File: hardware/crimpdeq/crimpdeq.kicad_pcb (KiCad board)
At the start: 2 copper layers, 54 parts, among them J2 USB4105-GF-A, Q1 S8550, Q2 DMG3415U, SW1 SW_Push, SW2 SW_Push, U1 ESP32-C3-MINI-1, U2 MCP73831T-2ACI/OT, U3 HX711, U4 Rust_Board, U6 SY8088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

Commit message: pcb: Initial placing of hx711
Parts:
- moved C10 114.2 mm to (142.5, 83.5)
- moved C9 112.8 mm to (139.2, 83.5)
- moved C12 108.5 mm to (143.8, 74.2), turned to 90 degrees
- moved C11 108.2 mm to (143.8, 71.0), turned to -90 degrees
- moved C13 106.0 mm to (144.6, 68.4), turned to 180 degrees
- moved R7 104.0 mm to (145.2, 74.8), turned to 90 degrees
- moved R8 103.8 mm to (145.8, 69.8), turned to 180 degrees
- moved R6 102.3 mm to (142.2, 77.0)
- moved R5 100.4 mm to (139.5, 77.0)
- moved J2 99.3 mm to (140.7, 104.4), turned to 180 degrees
- moved Q1 92.8 mm to (139.5, 80.5)
- moved U3 91.7 mm to (137.6, 72.4), turned to 90 degrees
- moved R10 8.25 mm to (147.0, 74.6), turned to 180 degrees
- moved C14 3.50 mm to (147.0, 75.8), turned to 180 degrees
- moved SW2 1.74 mm to (146.0, 80.0)
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
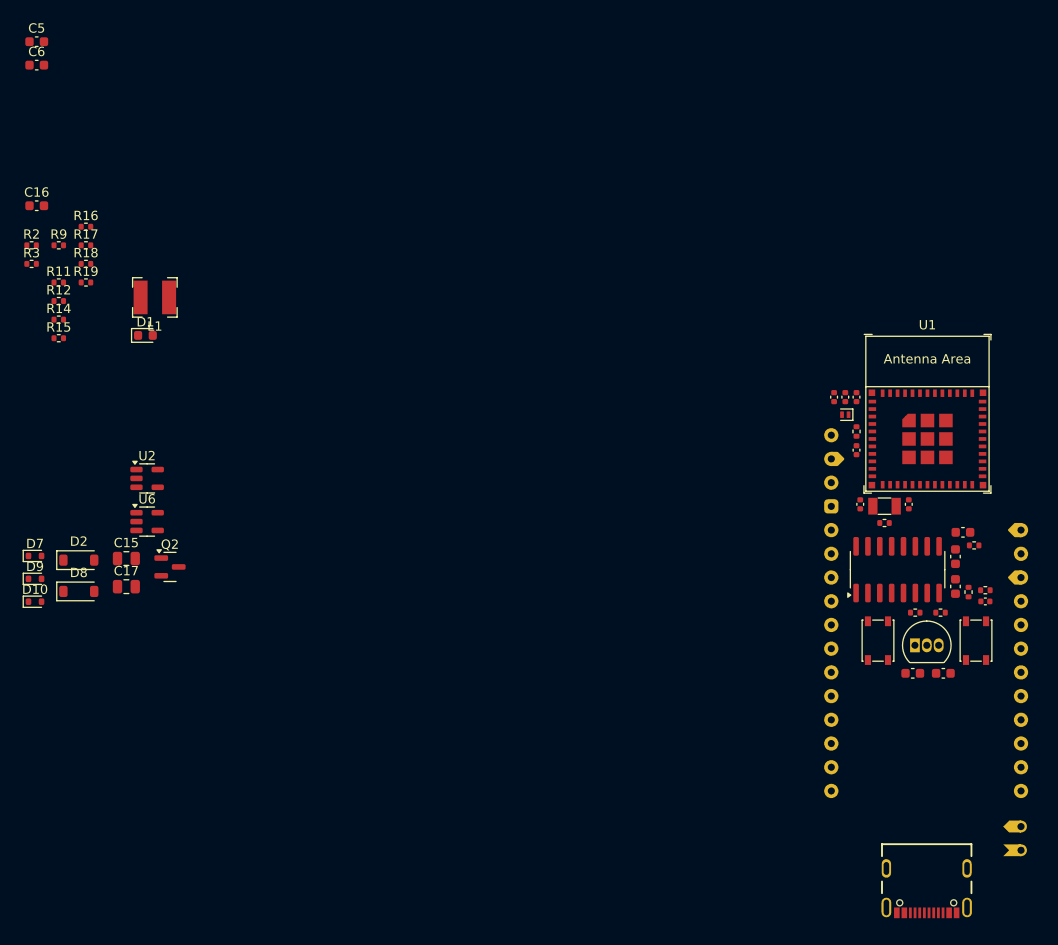
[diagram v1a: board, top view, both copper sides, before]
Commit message: pcb: Initial wiring of pcb
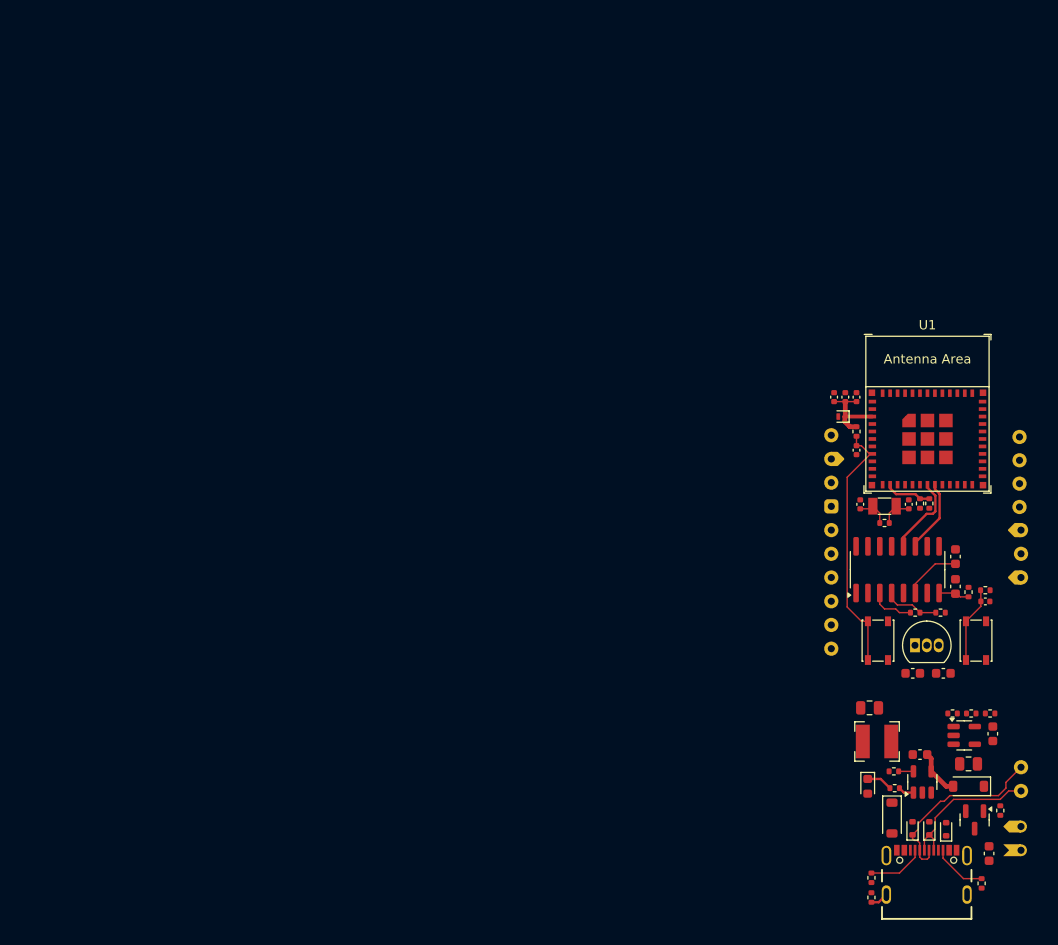
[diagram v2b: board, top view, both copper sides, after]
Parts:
- removed C13: 0.1uF, Capacitor_SMD:C_0603_1608Metric
- removed R8: 1kR 1%, Resistor_SMD:R_0402_1005Metric
- moved C6 132.4 mm to (147.4, 102.8), turned to -90 degrees
- moved C5 121.6 mm to (140.0, 92.2)
- moved R9 117.6 mm to (148.6, 98.2), turned to -90 degrees
- moved C16 117.0 mm to (147.8, 90.0), turned to -90 degrees
- moved R18 116.6 mm to (146.6, 106.0), turned to -90 degrees
- moved R17 109.3 mm to (134.8, 107.5), turned to 90 degrees
- moved R16 108.2 mm to (145.5, 87.8), turned to 180 degrees
- moved R2 108.2 mm to (137.2, 94.0)
- moved R3 108.2 mm to (137.3, 95.8), turned to 180 degrees
- moved R15 107.5 mm to (147.5, 87.8), turned to 180 degrees
- moved R19 105.6 mm to (134.8, 105.4), turned to -90 degrees
- moved R14 104.6 mm to (143.5, 87.8), turned to 180 degrees
- moved D9 101.2 mm to (142.8, 100.2), turned to 90 degrees
- moved D10 98.8 mm to (141.0, 100.1), turned to 90 degrees
- moved D7 98.4 mm to (139.2, 100.1), turned to 90 degrees
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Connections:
- C1 pad 2: GND -> E-
- C10 pad 1: Net-(Q1-C) -> E+
- C10 pad 2: GND -> E-
- C11 pad 1: GND -> E-
- C14 pad 1: GND -> E-
- C15 pad 2: GND -> E-
- C17 pad 2: GND -> E-
- C2 pad 2: GND -> E-
- C3 pad 2: GND -> E-
- C4 pad 2: GND -> E-
- C5 pad 1: GND -> E-
- C6 pad 2: GND -> E-
- C7 pad 2: GND -> E-
- C8 pad 2: GND -> E-
- C9 pad 2: GND -> E-
- D10 pad 2: GND -> E-
- D3 pad 2: GND -> E-
- D7 pad 2: GND -> E-
- D9 pad 2: GND -> E-
- J2 pad A1_B12: GND -> E-
- J2 pad B1_A12: GND -> E-
- Q1 pad 3: Net-(Q1-C) -> E+
- R11 pad 2: GND -> E-
- R16 pad 2: GND -> E-
- R17 pad 2: GND -> E-
- R18 pad 2: GND -> E-
- R19 pad 2: GND -> E-
- R2 pad 1: GND -> E-
- R5 pad 1: Net-(Q1-C) -> E+
- R6 pad 2: GND -> E-
- R9 pad 2: GND -> E-
- SW1 pad 2: GND -> E-
- SW2 pad 2: GND -> E-
- U1 pad 1: GND -> E-
- U1 pad 11: GND -> E-
- U1 pad 12: IO0 -> unconnected-(U1-GPIO0/ADC1_CH0/XTAL_32K_P-Pad12)
- U1 pad 14: GND -> E-
- U1 pad 16: IO10 -> unconnected-(U1-GPIO10-Pad16)
- U1 pad 2: GND -> E-
- U1 pad 20: IO6 -> unconnected-(U1-GPIO6-Pad20)
- U1 pad 21: IO7 -> unconnected-(U1-GPIO7-Pad21)
- U1 pad 22: IO8 -> unconnected-(U1-GPIO8-Pad22)
- U1 pad 36: GND -> E-
- U1 pad 5: IO2 -> unconnected-(U1-GPIO2/ADC1_CH2-Pad5)
- U1 pad 6: IO3 -> unconnected-(U1-GPIO3/ADC1_CH3-Pad6)
- U2 pad 2: GND -> E-
- U3 pad 10: Net-(U3-INB+) -> E-
- U3 pad 14: GND -> E-
- U3 pad 15: GND -> E-
- U3 pad 3: Net-(Q1-C) -> E+
- U3 pad 5: GND -> E-
- U3 pad 9: B- -> E-
- U4 pad 10: IO5_SCK -> IO9_BOOT
- U4 pad 11: IO6 -> USB_D+
- U4 pad 12: IO7 -> USB_D-
- U4 pad 13: IO8 -> VBUS
- U4 pad 14: IO21_TX -> ENABLE
- U4 pad 15: IO20_RX -> +BATT
- U4 pad 16: IO9_BOOT -> A+
- U4 pad 17: IO10 -> A-
- U4 pad 18: IO8 -> E-
- U4 pad 19: USB_D+ -> E+
- U4 pad 20: USB_D- -> E-
- U4 pad 21: unconnected-(U4-SPIQ/GPIO17-Pad21) -> +BATT
- U4 pad 4: GND -> E-
- U4 pad 5: IO0 -> IO1_ADC
- U4 pad 6: IO1_ADC -> IO4_DATA
- U4 pad 7: IO2 -> IO5_SCK
- U4 pad 8: IO3 -> IO21_TX
- U4 pad 9: IO4_DATA -> IO20_RX
- U6 pad 2: GND -> E-
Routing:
- net CHIP_PU: track 0.00 -> 27.7 mm
- net USB_D-: track 0.00 -> 20.1 mm
- net USB_D+: track 0.00 -> 16.2 mm
- net +3V3: track 0.00 -> 8.99 mm
- net IO4_DATA: track 0.00 -> 8.75 mm
- net IO9_BOOT: track 0.00 -> 8.15 mm
- net IO5_SCK: track 0.00 -> 7.88 mm
- net Net-(U3-VBG): track 0.00 -> 6.18 mm
- net Net-(J2-CC1): track 0.00 -> 6.14 mm
- net Net-(U3-VFB): track 0.00 -> 5.98 mm
- net Net-(J2-CC2): track 0.00 -> 5.89 mm
- net IO1_ADC: track 0.00 -> 5.04 mm
- net VBUS: track 0.00 -> 4.99 mm
- net E+: track 0.00 -> 4.85 mm
- net IO1: track 0.00 -> 3.57 mm
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
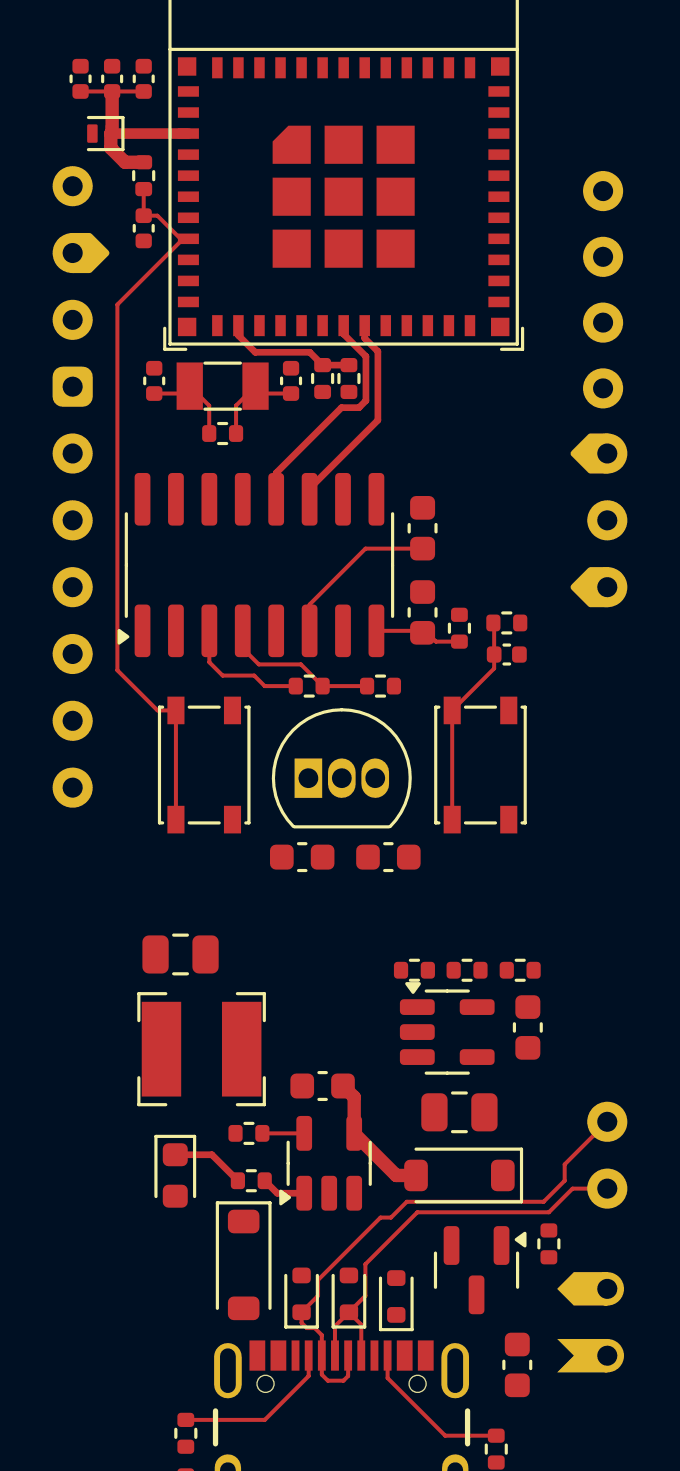
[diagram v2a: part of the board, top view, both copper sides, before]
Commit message: pcb: Remove unused exposed pins and connect hx711/RATE to 3.3v
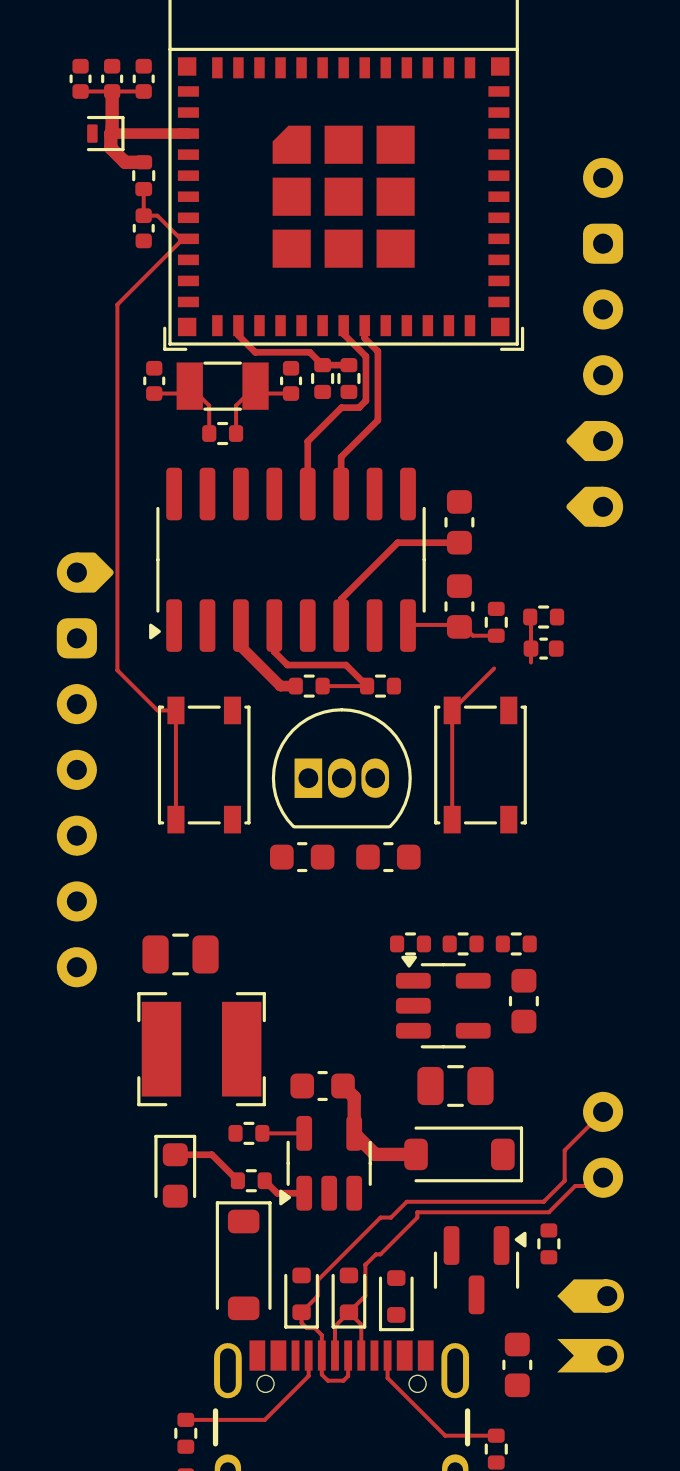
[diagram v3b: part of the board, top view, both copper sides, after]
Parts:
- moved C14 1.42 mm to (148.4, 75.6)
- moved R10 1.42 mm to (148.4, 74.4)
- moved R7 1.42 mm to (146.6, 74.6)
- moved C12 1.42 mm to (145.2, 74.0)
- moved C11 1.42 mm to (145.2, 70.8)
- moved U3 1.22 mm to (138.8, 72.2)
- moved C16 1.01 mm to (147.7, 89.0)
- moved R14 1.01 mm to (143.3, 86.8)
- moved R16 1.01 mm to (145.3, 86.8)
- moved U6 1.01 mm to (144.6, 89.2)
- moved C15 1.01 mm to (145.1, 92.2)
- moved R15 1.01 mm to (147.4, 86.8)
- moved D2 0.80 mm to (145.2, 94.8)
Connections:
- C1 pad 2: E- -> GND
- C10 pad 2: E- -> GND
- C11 pad 1: E- -> GND
- C14 pad 1: E- -> GND
- C15 pad 2: E- -> GND
- C17 pad 2: E- -> GND
- C2 pad 2: E- -> GND
- C3 pad 2: E- -> GND
- C4 pad 2: E- -> GND
- C5 pad 1: E- -> GND
- C6 pad 2: E- -> GND
- C7 pad 2: E- -> GND
- C8 pad 2: E- -> GND
- C9 pad 1: +3.3V -> +3V3
- C9 pad 2: E- -> GND
- D10 pad 2: E- -> GND
- D3 pad 2: E- -> GND
- D7 pad 2: E- -> GND
- D9 pad 2: E- -> GND
- J2 pad A1_B12: E- -> GND
- J2 pad B1_A12: E- -> GND
- Q1 pad 1: +3.3V -> +3V3
- R11 pad 2: E- -> GND
- R16 pad 2: E- -> GND
- R17 pad 2: E- -> GND
- R18 pad 2: E- -> GND
- R19 pad 2: E- -> GND
- R2 pad 1: E- -> GND
- R6 pad 2: E- -> GND
- R9 pad 2: E- -> GND
- SW1 pad 2: E- -> GND
- SW2 pad 2: E- -> GND
- U1 pad 1: E- -> GND
- U1 pad 11: E- -> GND
- U1 pad 14: E- -> GND
- U1 pad 2: E- -> GND
- U1 pad 36: E- -> GND
- U1 pad 49: (no net) -> GND
- U2 pad 2: E- -> GND
- U3 pad 1: +3.3V -> +3V3
- U3 pad 10: E- -> GND
- U3 pad 14: E- -> GND
- U3 pad 15: E- -> +3V3
- U3 pad 16: +3.3V -> +3V3
- U3 pad 5: E- -> GND
- U3 pad 9: E- -> GND
- U4 pad 1: CHIP_PU -> +3V3
- U4 pad 10: IO9_BOOT -> VBUS
- U4 pad 11: USB_D+ -> +BATT
- U4 pad 12: USB_D- -> A+
- U4 pad 13: VBUS -> A-
- U4 pad 14: ENABLE -> GND
- U4 pad 15: +BATT -> E+
- U4 pad 16: A+ -> GND
- U4 pad 17: A- -> +BATT
- U4 pad 2: +3V3 -> GND
- U4 pad 3: unconnected-(U4-N/C-Pad3) -> IO1_ADC
- U4 pad 4: E- -> IO4_DATA
- U4 pad 5: IO1_ADC -> IO5_SCK
- U4 pad 6: IO4_DATA -> IO21_TX
- U4 pad 7: IO5_SCK -> IO20_RX
- U4 pad 8: IO21_TX -> USB_D-
- U4 pad 9: IO20_RX -> USB_D+
- U6 pad 2: E- -> GND
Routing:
- net unconnected-(U3-XO-Pad13): track 0.00 -> 1.00 mm
- net GND: track 0.00 -> 1.00 mm
- net Net-(U3-VFB): track 5.98 -> 6.75 mm
- net IO5_SCK: track 7.88 -> 7.19 mm
- net E+: track 4.85 -> 4.17 mm
- net VBUS: track 4.99 -> 4.48 mm

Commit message: pcb: Update layout
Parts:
- moved R12 1.62 mm to (139.8, 66.4)
- moved R11 0.65 mm to (140.4, 64.8), turned to 0 degrees
- moved R16 0.40 mm to (145.3, 86.4), turned to 90 degrees
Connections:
- U1 pad 49: GND -> (no net)
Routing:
- net +BATT: track 0.00 -> 69.7 mm, vias 0 -> 6
- net +3V3: track 8.99 -> 77.7 mm, vias 0 -> 1
- net USB_D+: track 16.3 -> 55.2 mm, vias 0 -> 5
- net USB_D-: track 20.5 -> 57.7 mm, vias 0 -> 5
- net VBUS: track 4.48 -> 36.9 mm, vias 0 -> 3
- net E+: track 4.17 -> 22.0 mm, vias 0 -> 1
- net GND: track 1.00 -> 18.2 mm, vias 0 -> 7
- net Net-(D8-A): track 0.00 -> 16.4 mm, vias 0 -> 2
- net IO9_BOOT: track 8.15 -> 22.0 mm, vias 0 -> 2
- net +5V: track 0.00 -> 13.5 mm
- net IO4_DATA: track 8.47 -> 20.4 mm, vias 0 -> 1
- net A-: track 0.00 -> 11.1 mm
- net IO5_SCK: track 7.19 -> 16.2 mm
- net Net-(Q1-B): track 0.00 -> 8.49 mm
- net IO1_ADC: track 5.04 -> 12.4 mm, vias 0 -> 1
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- added copper zone on F.Cu, net +3V3
- added copper zone on F.Cu, net +5V
- added copper zone on F.Cu, net +BATT
- added copper zone on F.Cu, net /Buck_Coil
- added copper zone on B.Cu, net GND
- added copper zone on F.Cu, net GND

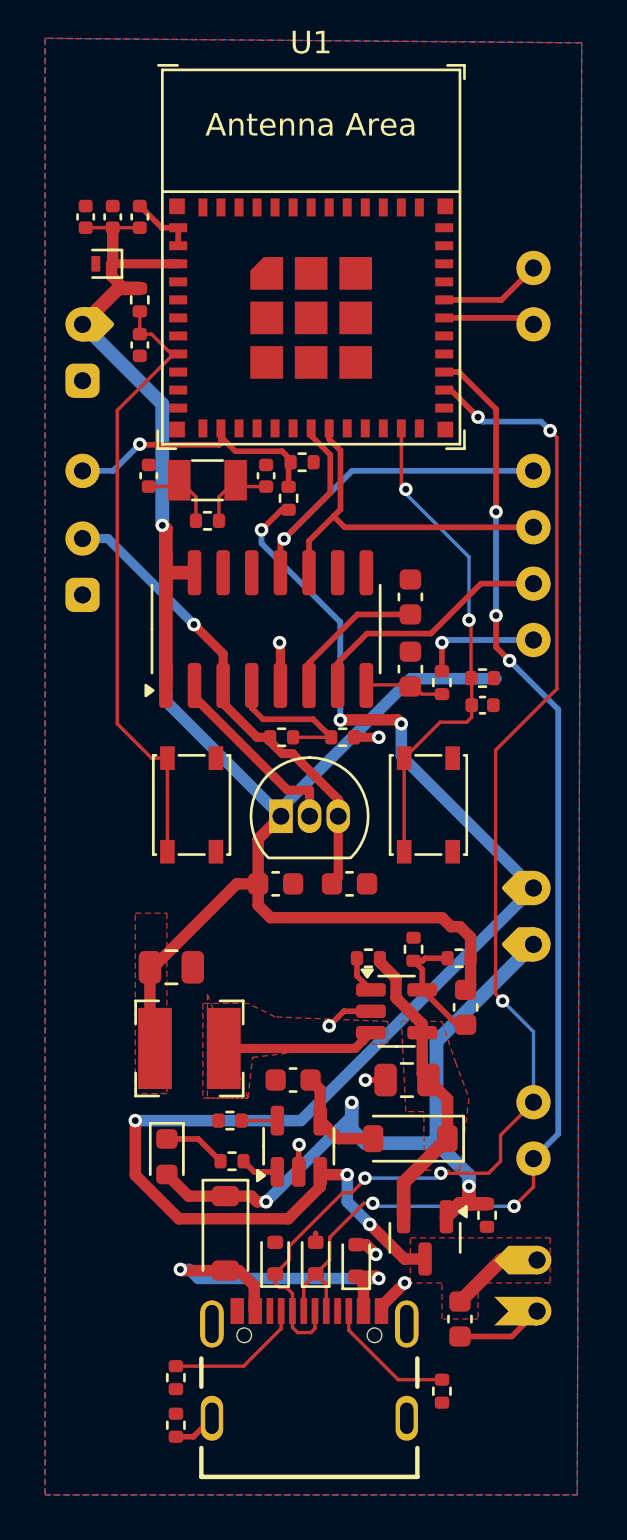
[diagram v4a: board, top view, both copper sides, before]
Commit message: pcb: Fix DRC unconnected items
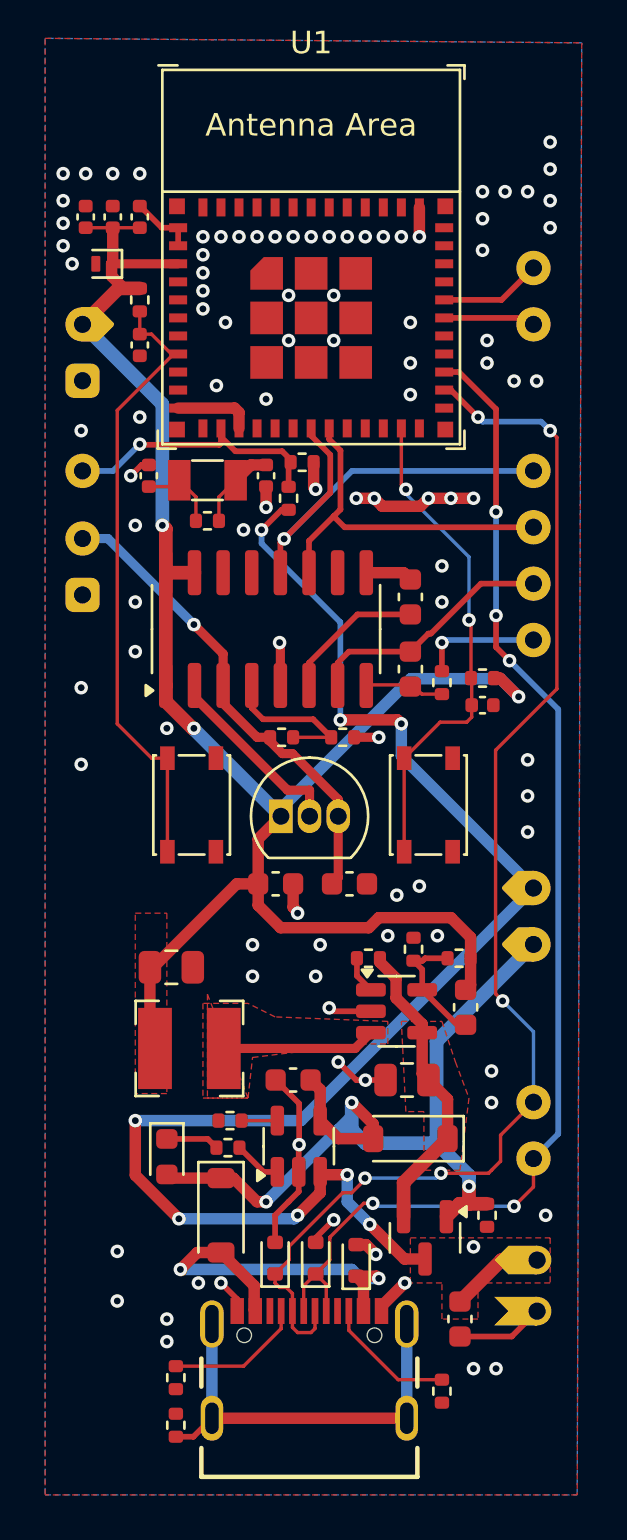
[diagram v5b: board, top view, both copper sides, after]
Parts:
- moved D8 0.82 mm to (136.8, 98.2)
- moved R3 0.63 mm to (137.1, 95.2)
- turned C8 to -90 degrees
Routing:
- net GND: track 18.2 -> 45.7 mm, vias 7 -> 100
- net Net-(J2-SHELL_GND-PadS1): track 1.94 -> 18.9 mm
- net +3V3: track 77.7 -> 81.3 mm, vias 1 -> 3
- net VBUS: track 36.9 -> 38.9 mm
- net Net-(D8-A): track 16.4 -> 17.1 mm
- net IO1: track 3.57 -> 4.13 mm
- net +BATT: track 69.7 -> 69.8 mm, vias 6 -> 8
